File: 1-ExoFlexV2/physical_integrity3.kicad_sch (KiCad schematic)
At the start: 27 parts, among them J123 Jumper, J124 Jumper, J125 Jumper, J126 Jumper, J127 Jumper, J128 Jumper, J129 Jumper, U100 OR Gate, U101 OR Gate, U102 OR Gate, U103 OR Gate, U98 OR Gate, U99 OR Gate

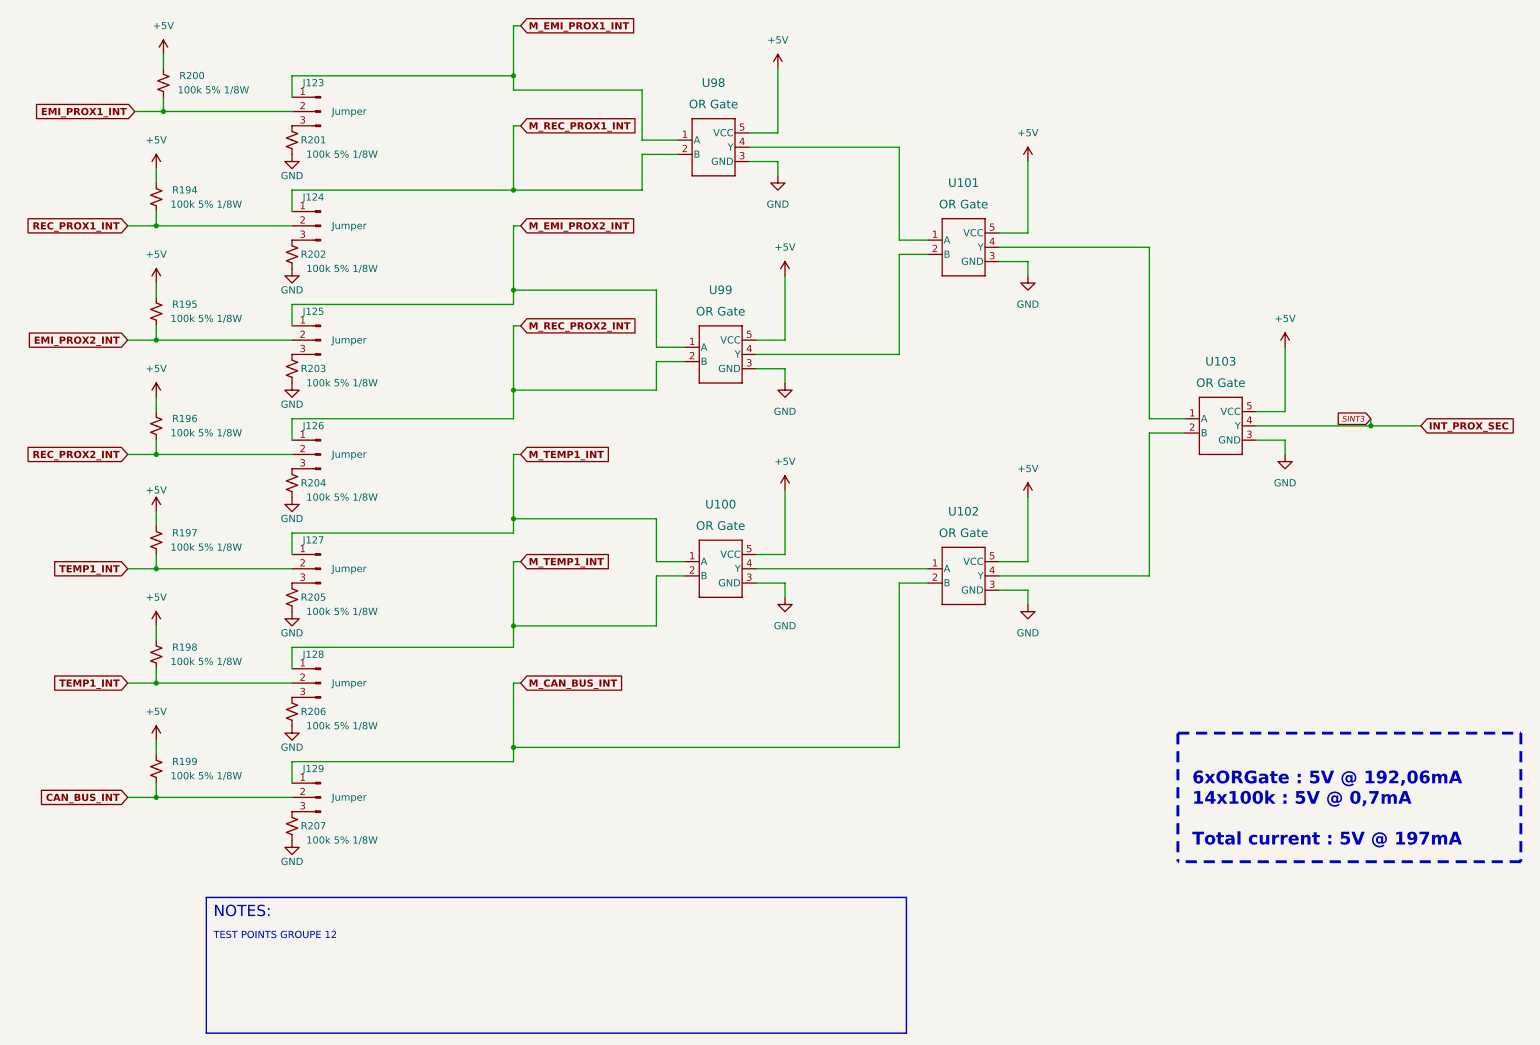
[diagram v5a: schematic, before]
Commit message: Finalisation 3
- Changement des régulateur de tension
- Retrait de test point inutile
- Changement de jumper mal positionner
- Ajout de Mounting holes et fiducial
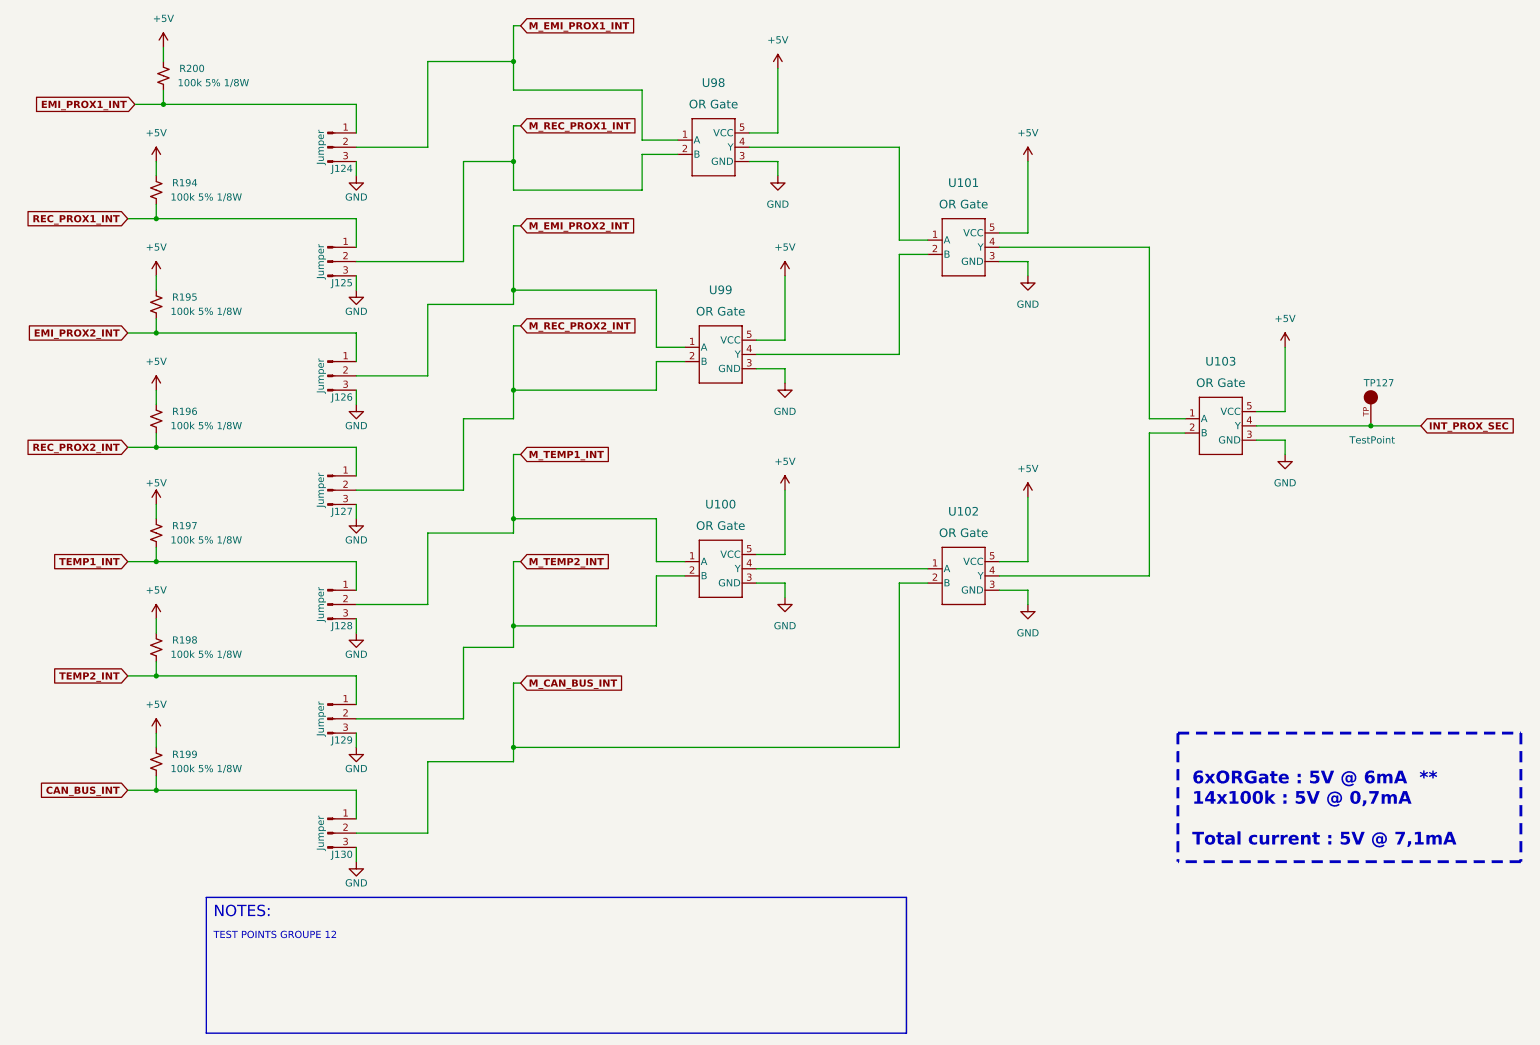
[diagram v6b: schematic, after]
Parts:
- removed R201, R202, R203, R204, R205, R206, R207: 100k 5% 1/8W, Resistor_SMD:R_0805_2012Metric, symbol Device:R_Small_US
- added TP127: TestPoint, FootPrint:KEYSTONE_5005, symbol SymLib:5005
- J124: renamed from J123; footprint Connector_PinSocket_2.54mm:PinSocket_1x03_P2.54mm_Vertical -> Connector_PinHeader_2.54mm:PinHeader_1x03_P2.54mm_Vertical
- J125: renamed from J124; footprint Connector_PinSocket_2.54mm:PinSocket_1x03_P2.54mm_Vertical -> Connector_PinHeader_2.54mm:PinHeader_1x03_P2.54mm_Vertical
- J126: renamed from J125; footprint Connector_PinSocket_2.54mm:PinSocket_1x03_P2.54mm_Vertical -> Connector_PinHeader_2.54mm:PinHeader_1x03_P2.54mm_Vertical
- J127: renamed from J126; footprint Connector_PinSocket_2.54mm:PinSocket_1x03_P2.54mm_Vertical -> Connector_PinHeader_2.54mm:PinHeader_1x03_P2.54mm_Vertical
- J128: renamed from J127; footprint Connector_PinSocket_2.54mm:PinSocket_1x03_P2.54mm_Vertical -> Connector_PinHeader_2.54mm:PinHeader_1x03_P2.54mm_Vertical
- J129: renamed from J128; footprint Connector_PinSocket_2.54mm:PinSocket_1x03_P2.54mm_Vertical -> Connector_PinHeader_2.54mm:PinHeader_1x03_P2.54mm_Vertical
- J130: renamed from J129; footprint Connector_PinSocket_2.54mm:PinSocket_1x03_P2.54mm_Vertical -> Connector_PinHeader_2.54mm:PinHeader_1x03_P2.54mm_Vertical
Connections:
- net CAN_BUS_INT: now also J130.1 (Pin_1); no longer J130.2 (Pin_2)
- net EMI_PROX1_INT: now also J124.1 (Pin_1); no longer J124.2 (Pin_2)
- net EMI_PROX2_INT: now also J126.1 (Pin_1); no longer J126.2 (Pin_2)
- net GND: now also J124.3 (Pin_3), J125.3 (Pin_3), J126.3 (Pin_3), J127.3 (Pin_3), J128.3 (Pin_3), J129.3 (Pin_3), J130.3 (Pin_3)
- net INT_PROX_SEC: now also TP127.TP
- net M_CAN_BUS_INT: now also J130.2 (Pin_2); no longer J130.1 (Pin_1)
- net M_EMI_PROX1_INT: now also J124.2 (Pin_2); no longer J124.1 (Pin_1)
- net M_EMI_PROX2_INT: now also J126.2 (Pin_2); no longer J126.1 (Pin_1)
- net M_REC_PROX1_INT: now also J125.2 (Pin_2); no longer J125.1 (Pin_1)
- net M_REC_PROX2_INT: now also J127.2 (Pin_2); no longer J127.1 (Pin_1)
- net M_TEMP1_INT: now also J128.2 (Pin_2); no longer J128.1 (Pin_1), J129.1 (Pin_1), U100.2 (B)
- net REC_PROX1_INT: now also J125.1 (Pin_1); no longer J125.2 (Pin_2)
- net REC_PROX2_INT: now also J127.1 (Pin_1); no longer J127.2 (Pin_2)
- net TEMP1_INT: now also J128.1 (Pin_1); no longer J128.2 (Pin_2), J129.2 (Pin_2), R198.2
- new net M_TEMP2_INT: J129.2 (Pin_2), U100.2 (B)
- new net TEMP2_INT: J129.1 (Pin_1), R198.2
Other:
- note added: "6xORGate : 5V @ 6mA ** 14x100k : 5V @ 0,7mA Total current : 5V @ 7,1mA"
- note removed: "6xORGate : 5V @ 192,06mA 14x100k : 5V @ 0,7mA Total current : 5V @ 197mA"
- moved on the sheet: J124, J125, J126, J127, J128, J129, J130, R194, R195, R196, R197, R198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

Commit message: Finalisation schéma FIN
- Changement des uméro pour les inverseurs
- Changement des connecteur et début de placement
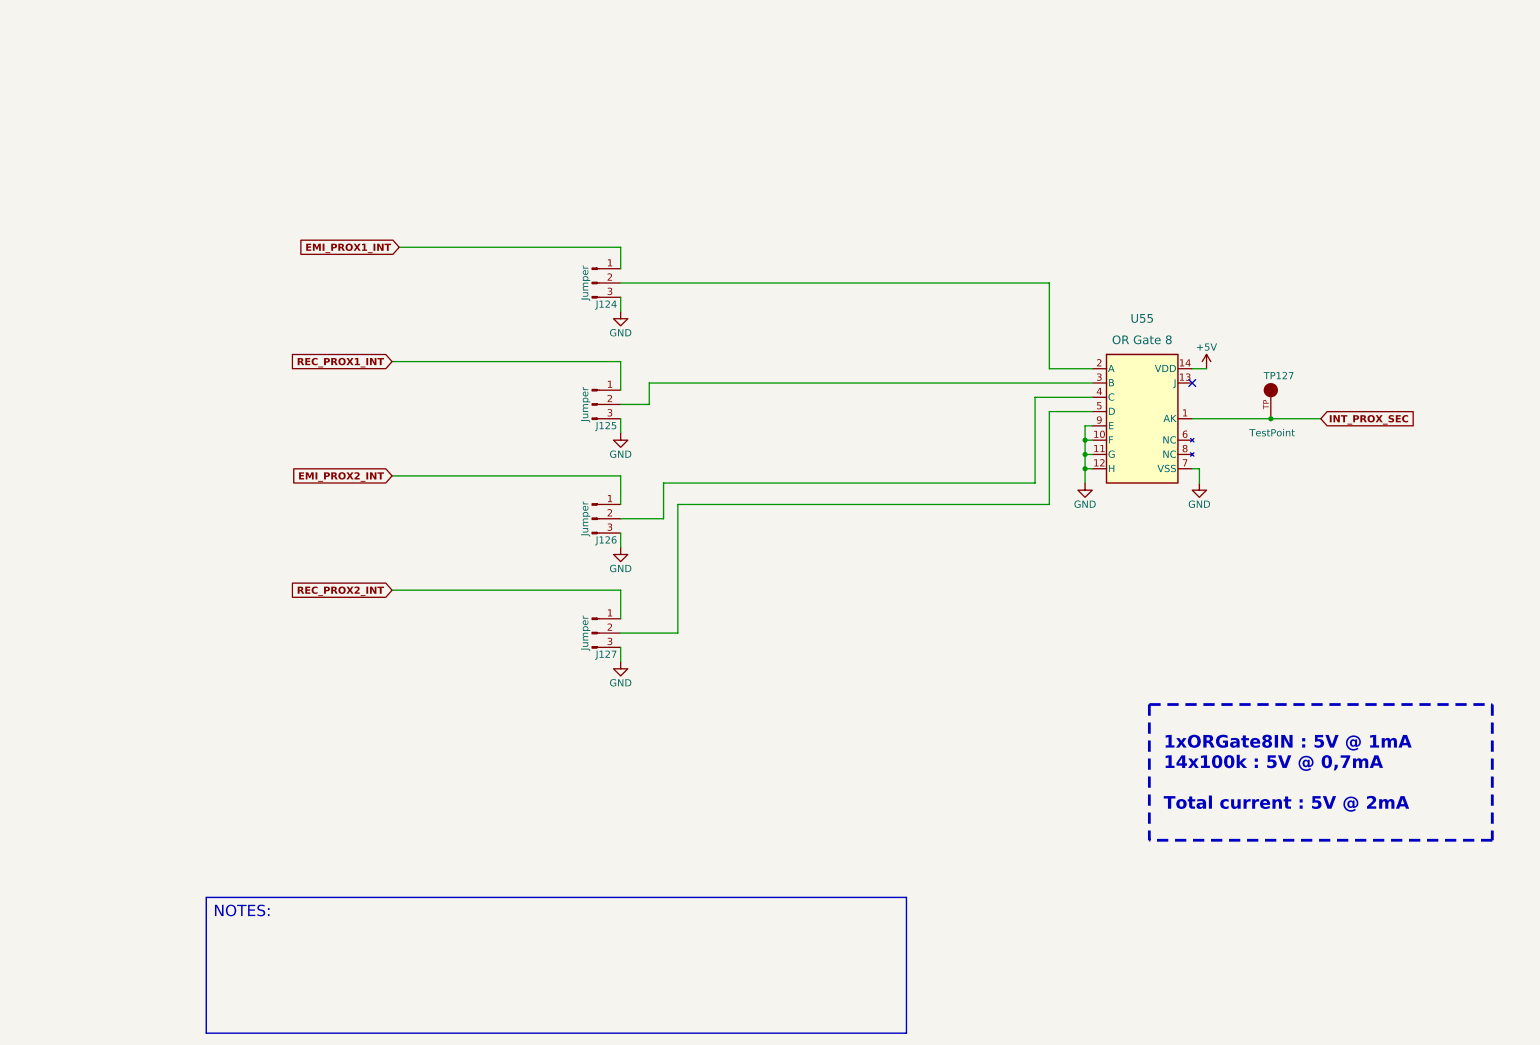
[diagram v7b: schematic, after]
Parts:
- removed J128, J129, J130: Jumper, Connector_PinHeader_2.54mm:PinHeader_1x03_P2.54mm_Vertical, symbol Connector:Conn_01x03_Male
- removed R194, R195, R196, R197, R198, R199, R200: 100k 5% 1/8W, Resistor_SMD:R_0805_2012Metric, symbol Device:R_Small_US
- removed U100, U101, U102, U103, U98, U99: OR Gate, FootPrint:SOT95P270X145-5N, symbol SymLib:SN74LVC1G32DBVR
- added U55: OR Gate 8, FootPrint:D14, symbol SymLib:CD4078BM96
- TP127: NOTES (none) -> DO NOT POPULATE; PURCHASE-URL https://pricing.snapeda.com/search/part/5005/?ref=eda -> (none)
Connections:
- net +5V: now also U55.14 (VDD)
- net GND: now also U55.10 (F), U55.11 (G), U55.12 (H), U55.7 (VSS), U55.9 (E)
- net INT_PROX_SEC: now also U55.1 (AK)
- net M_EMI_PROX1_INT: no longer names the net of J124.2 (Pin_2)
- net M_EMI_PROX1_INT: now also U55.2 (A)
- net M_EMI_PROX2_INT: no longer names the net of J126.2 (Pin_2)
- net M_EMI_PROX2_INT: now also U55.4 (C)
- net M_REC_PROX1_INT: no longer names the net of J125.2 (Pin_2)
- net M_REC_PROX1_INT: now also U55.3 (B)
- net M_REC_PROX2_INT: no longer names the net of J127.2 (Pin_2)
- net M_REC_PROX2_INT: now also U55.5 (D)
- no-connect marks 0 -> 1
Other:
- note added: "1xORGate8IN : 5V @ 1mA 14x100k : 5V @ 0,7mA Total current : 5V @ 2mA"
- note removed: "6xORGate : 5V @ 6mA ** 14x100k : 5V @ 0,7mA Total current : 5V @ 7,1mA"
- note removed: "TEST POINTS GROUPE 12"
- moved on the sheet: J124, J125, J126, J127, TP127

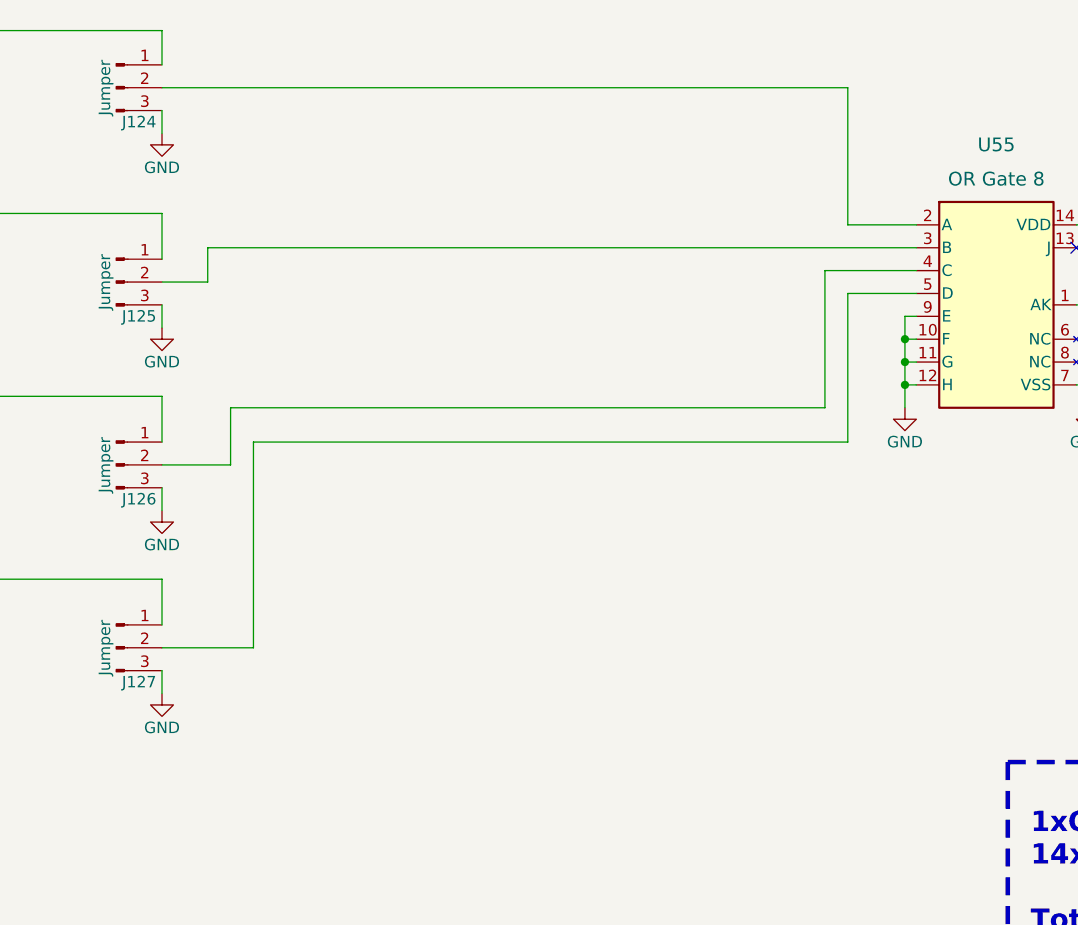
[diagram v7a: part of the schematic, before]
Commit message: Routage pour Review 1
- Replacement des test point pour faciliter le rework
- Correction des erreurs dans le BOM
-
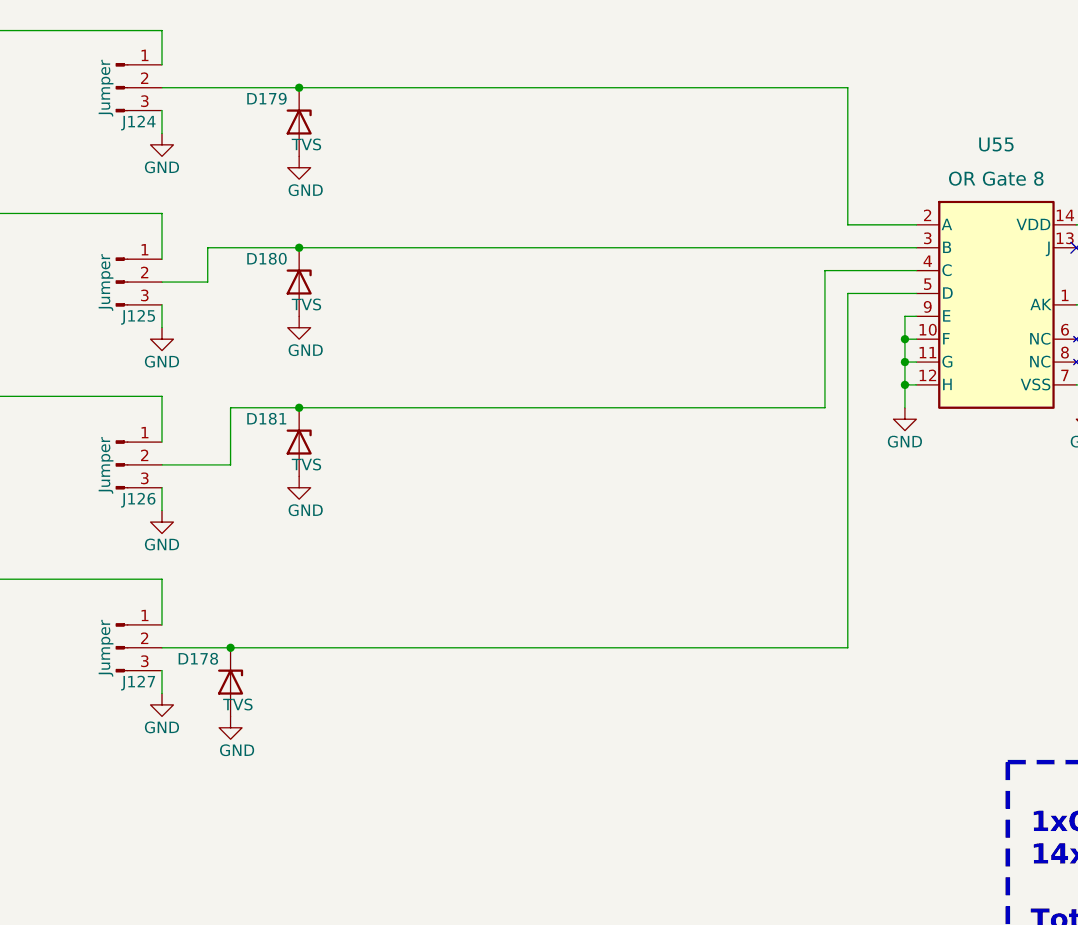
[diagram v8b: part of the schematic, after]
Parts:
- added D178, D179, D180, D181: TVS, FootPrint:DPY2_TEX, symbol Device:D_Zener
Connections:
- net GND: now also D178.2 (A), D179.2 (A), D180.2 (A), D181.2 (A)
- net at J124.2 (Pin_2), U55.2 (A): now also D179.1 (K)
- net at J125.2 (Pin_2), U55.3 (B): now also D180.1 (K)
- net at J126.2 (Pin_2), U55.4 (C): now also D181.1 (K)
- net at J127.2 (Pin_2), U55.5 (D): now also D178.1 (K)
